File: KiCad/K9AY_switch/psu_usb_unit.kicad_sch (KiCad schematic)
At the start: 31 parts, among them J4 12V, J5 USB_B_Micro, U11 CH340C, U12 USBLC6, U5 K7803-500R3, U6 K7805-500R3

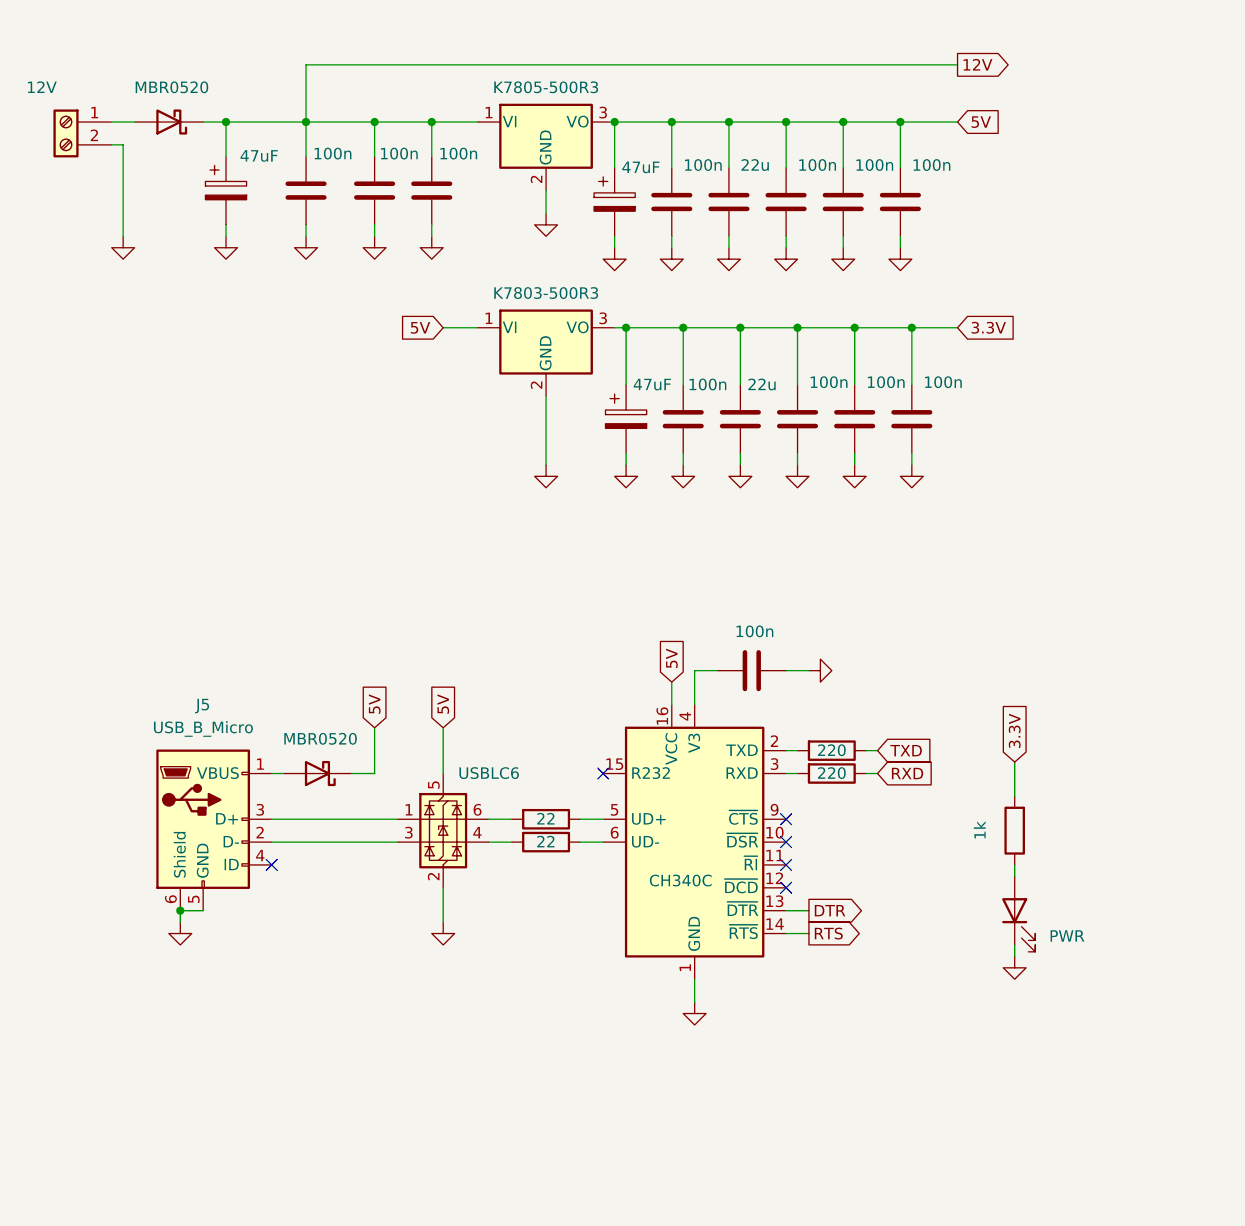
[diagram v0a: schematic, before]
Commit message: Update KiCad project, gerbers and pictures
- updated schematic, PCB, BOM, gerbers and plots
- new photos: k1, mosfet, pwr; updated direction diagram
- ignore KiCad backups, *.tar.gz and k9ay_v5.zip

Co-Authored-By: Claude Opus 5.5 <noreply@anthropic.com>
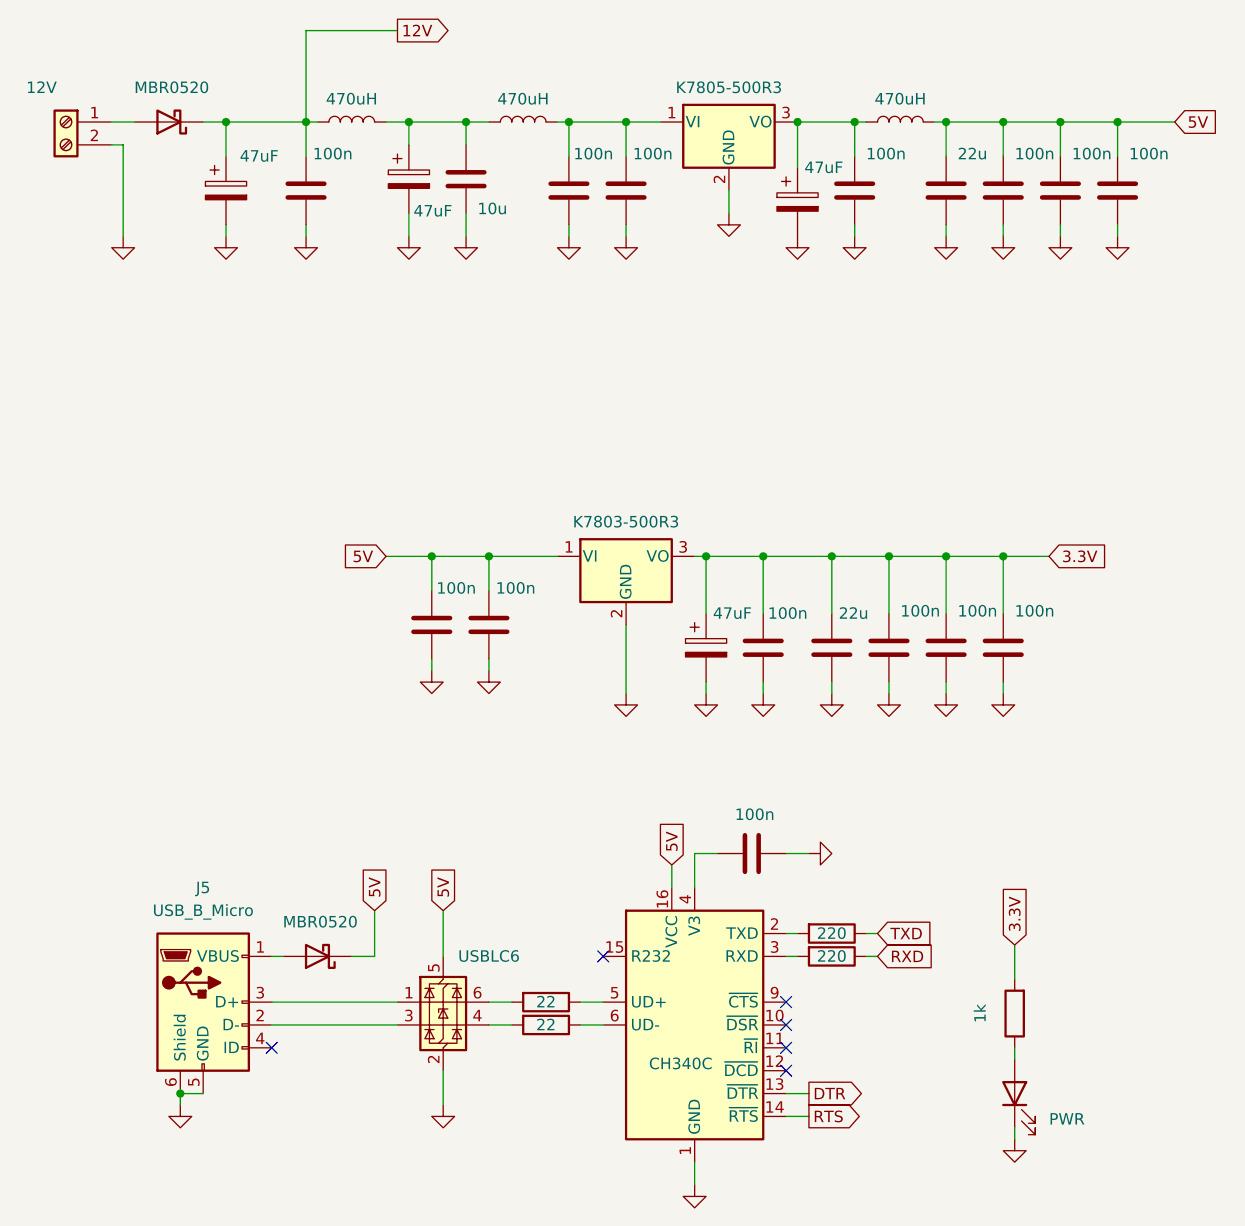
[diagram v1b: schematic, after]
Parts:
- added C30: 47uF, Capacitor_THT:CP_Radial_D5.0mm_P2.50mm, symbol Device:C_Polarized
- added C32: 10u, Capacitor_SMD:C_1206_3216Metric, symbol Device:C
- added C35, C36: 100n, Capacitor_SMD:C_1206_3216Metric, symbol Device:C
- added L2, L3, L4: 470uH, Inductor_THT:L_Radial_D10.0mm_P5.00mm_Neosid_SD12_style3, symbol Device:L
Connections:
- net 12V: now also L3.1; no longer C22.1, C23.1, U6.1 (VI)
- net 5V: now also C35.1, C36.1, L4.2; no longer C10.1, C11.1, U6.3 (VO)
- net GND: now also C30.2, C32.2, C35.2, C36.2
- new net: C22.1, C23.1, L2.2, U6.1 (VI)
- new net: C10.1, C11.1, L4.1, U6.3 (VO)
- new net: C30.1, C32.1, L2.1, L3.2
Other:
- moved on the sheet: J5
